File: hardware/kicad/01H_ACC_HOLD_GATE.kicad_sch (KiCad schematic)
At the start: 17 parts, among them Q912 MMBT5551, Q914 PMBT5551,215, Q915 MMBT5401-7-F, U911 140356145000 HOLD

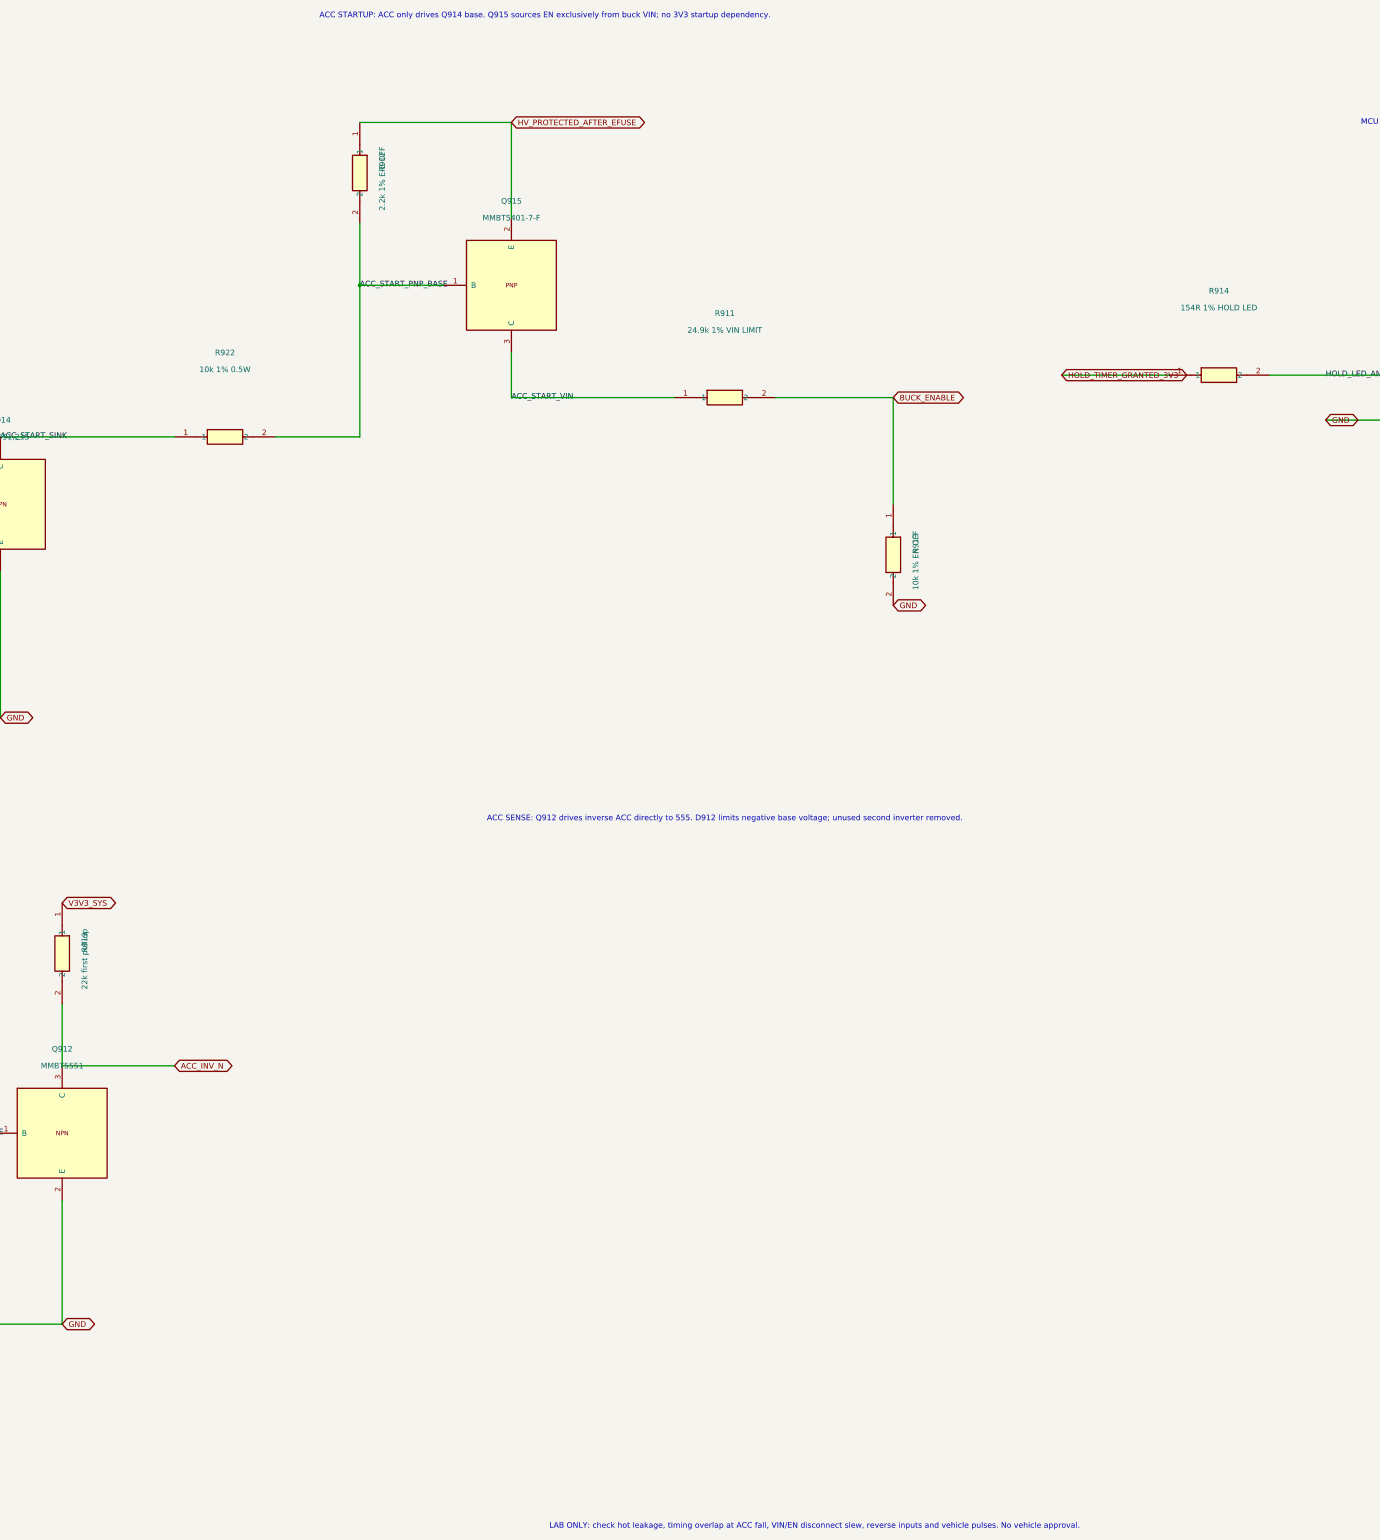
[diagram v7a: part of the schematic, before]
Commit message: hardware(acc): feed startup EN from clamped pre-FET VS to avoid LM74800 power-up deadlock
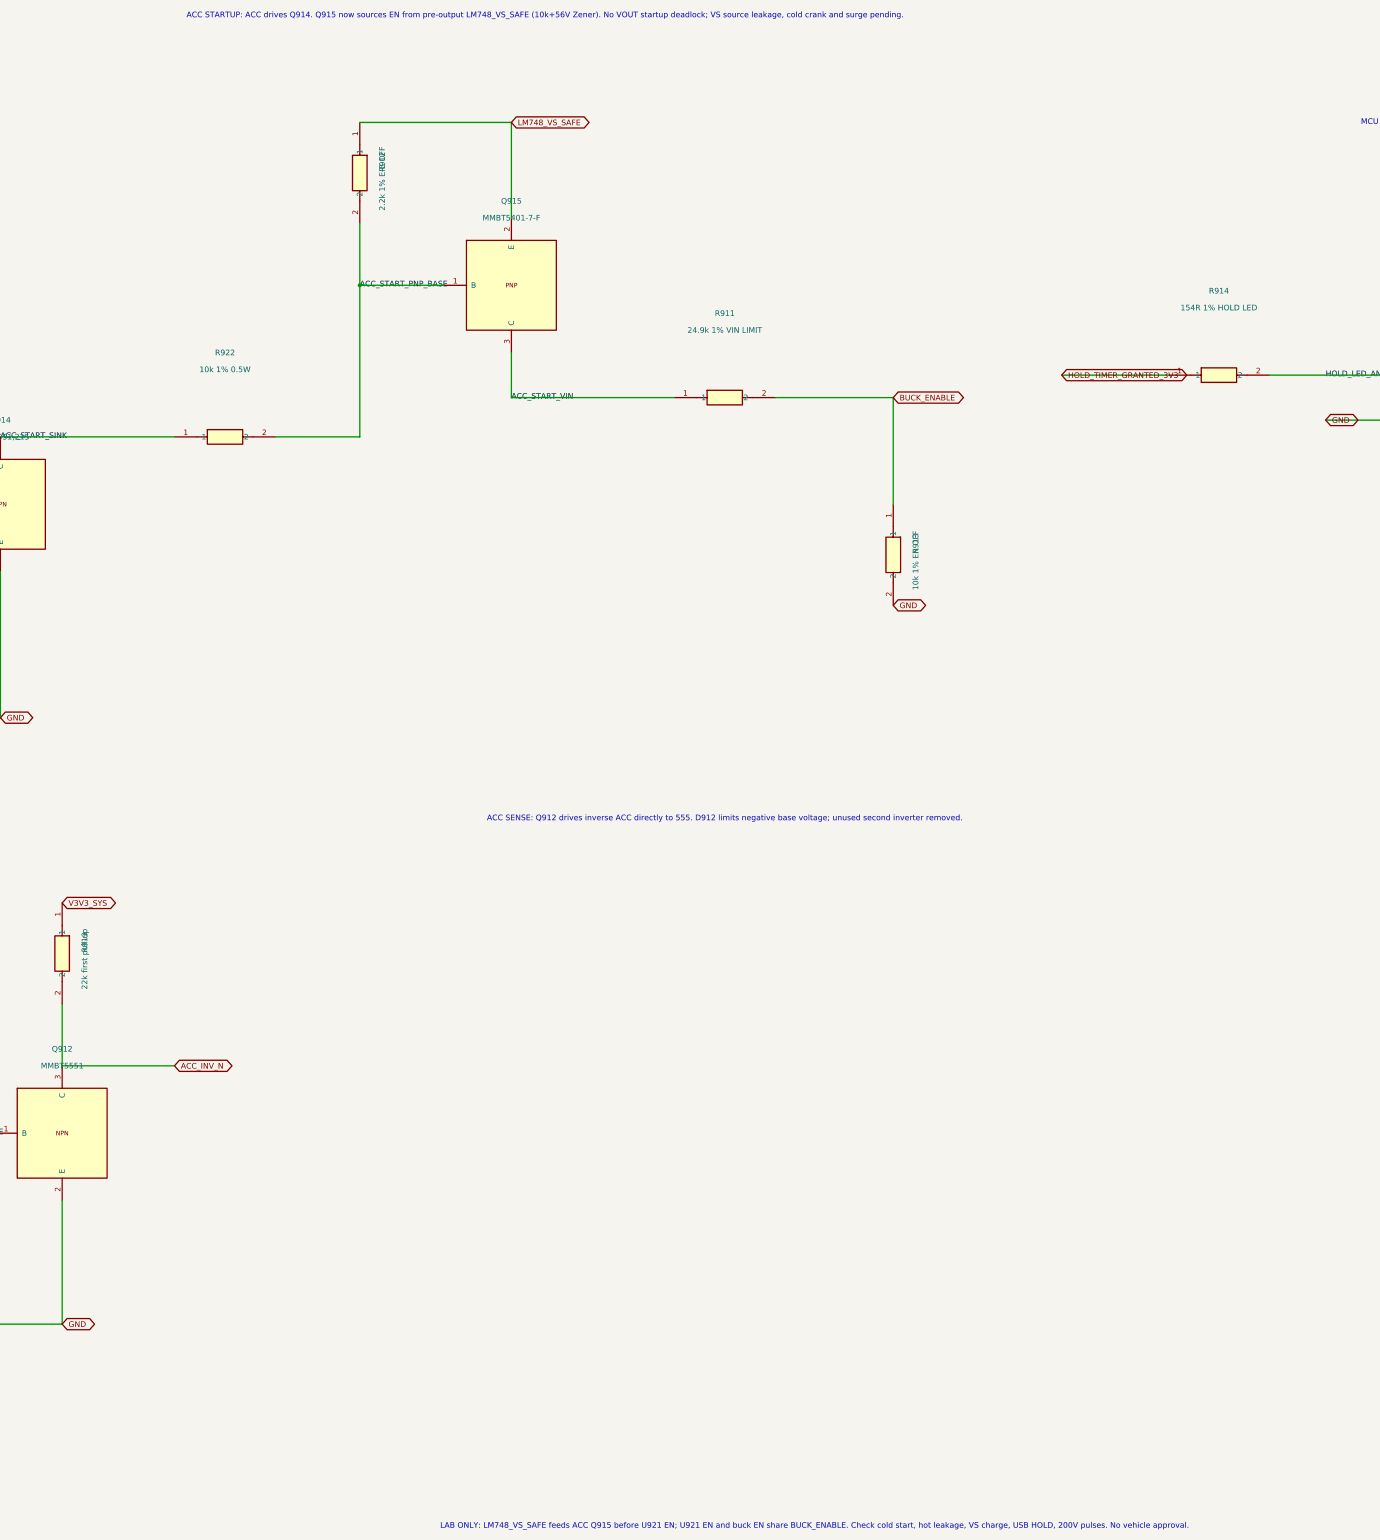
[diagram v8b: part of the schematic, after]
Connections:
- net HV_PROTECTED_AFTER_EFUSE: no longer Q915.2 (E), R912.1
- new net LM748_VS_SAFE: Q915.2 (E), R912.1
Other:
- note added: "ACC STARTUP: ACC drives Q914. Q915 now sources EN from pre-output LM748_VS_SAFE (10k+56V Zener). No VOUT startup deadlock; VS source leakage, cold crank and surge pending."
- note added: "LAB ONLY: LM748_VS_SAFE feeds ACC Q915 before U921 EN; U921 EN and buck EN share BUCK_ENABLE. Check cold start, hot leakage, VS charge, USB HOLD, 200V pulses. No vehicle approval."
- note removed: "ACC STARTUP: ACC only drives Q914 base. Q915 sources EN exclusively from buck VIN; no 3V3 startup dependency."
- note removed: "LAB ONLY: check hot leakage, timing overlap at ACC fall, VIN/EN disconnect slew, reverse inputs and vehicle pulses. No vehicle approval."
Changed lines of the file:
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@@
 (kicad_sch (version 20250114) (generator "eeschema") (paper "A2")
 (title_block (title "TripTracer ACC startup referenced to buck VIN / bounded MCU HOLD") (date "2026-10-14") (rev "c0 electrical correction / LAB ONLY"))
-(text "ACC STARTUP: ACC only drives Q914 base. Q915 sources EN exclusively from buck VIN; no 3V3 startup dependency." (at 223.52 24.13 0) (effects (font (size 1.27 1.27))))
+(text "ACC STARTUP: ACC drives Q914. Q915 now sources EN from pre-output LM748_VS_SAFE (10k+56V Zener). No VOUT startup deadlock; VS source leakage, cold crank and surge pending." (at 223.52 24.13 0) (effects (font (size 1.27 1.27))))
 (symbol (lib_id "TripTracer_V1:PMBT5551_ACC") (at 100.33 134.62 0) (unit 1) (in_bom yes) (on_board yes) (dnp no)
 (property "Reference" "Q914" (at 100.33 115.57 0) (effects (font (size 1.27 1.27))))
@@
 (wire (pts (xy 181.61 48.26) (xy 215.9 48.26)) (stroke (width 0) (type default)))
 (wire (pts (xy 215.9 48.26) (xy 215.9 69.85)) (stroke (width 0) (type default)))
-(global_label "HV_PROTECTED_AFTER_EFUSE" (shape bidirectional) (at 215.9 48.26 0) (effects (font (size 1.27 1.27)) (justify left)))
+(global_label "LM748_VS_SAFE" (shape bidirectional) (at 215.9 48.26 0) (effects (font (size 1.27 1.27)) (justify left)))
 (wire (pts (xy 215.9 100.33) (xy 215.9 110.49)) (stroke (width 0) (type default)))
 (wire (pts (xy 215.9 110.49) (xy 252.73 110.49)) (stroke (width 0) (type default)))
@@
 (wire (pts (xy 114.3 261.62) (xy 139.7 261.62)) (stroke (width 0) (type default)))
 (global_label "ACC_INV_N" (shape bidirectional) (at 139.7 261.62 0) (effects (font (size 1.27 1.27))))
-(text "LAB ONLY: check hot leakage, timing overlap at ACC fall, VIN/EN disconnect slew, reverse inputs and vehicle pulses. No vehicle approval." (at 284.48 365.76 0) (effects (font (size 1.27 1.27))))
+(text "LAB ONLY: LM748_VS_SAFE feeds ACC Q915 before U921 EN; U921 EN and buck EN share BUCK_ENABLE. Check cold start, hot leakage, VS charge, USB HOLD, 200V pulses. No vehicle approval." (at 284.48 365.76 0) (effects (font (size 1.27 1.27))))
 (sheet_instances (path "/" (page "1")))
 (symbol (lib_id "TripTracer_V1:BAT54WS_CLAMP") (at 60.96 308.61 90) (unit 1) (in_bom yes) (on_board yes) (dnp no)
